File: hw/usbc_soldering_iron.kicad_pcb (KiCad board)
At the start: 4 copper layers, 70 x 30 mm, 82 parts, among them J1 U263-163N-4OS1735, J16 TIP_CONN, J2 DBG, J3 OLED, J4 GPIO, J5 DISP, Q1 AGM403AP, U1 SC7A20, U10 TPA191Ax, U2 CH32X035F8U6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

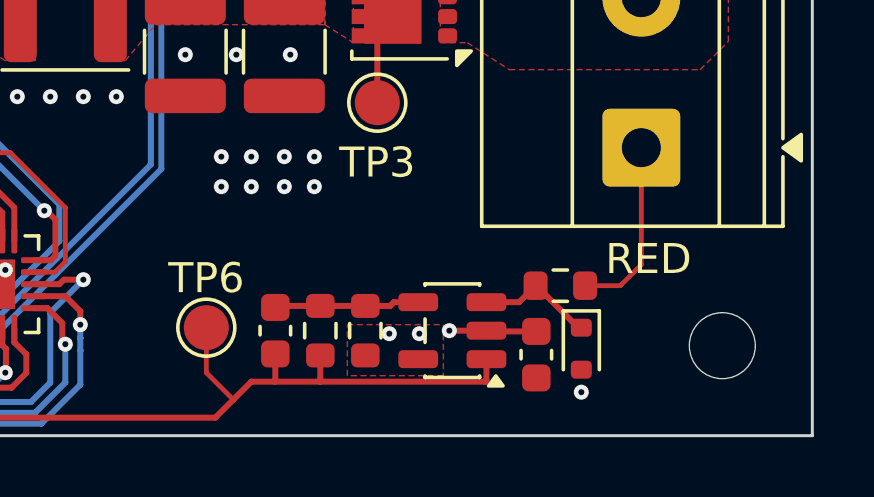
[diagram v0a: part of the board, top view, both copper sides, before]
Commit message: corrected tlv333 pin assignment
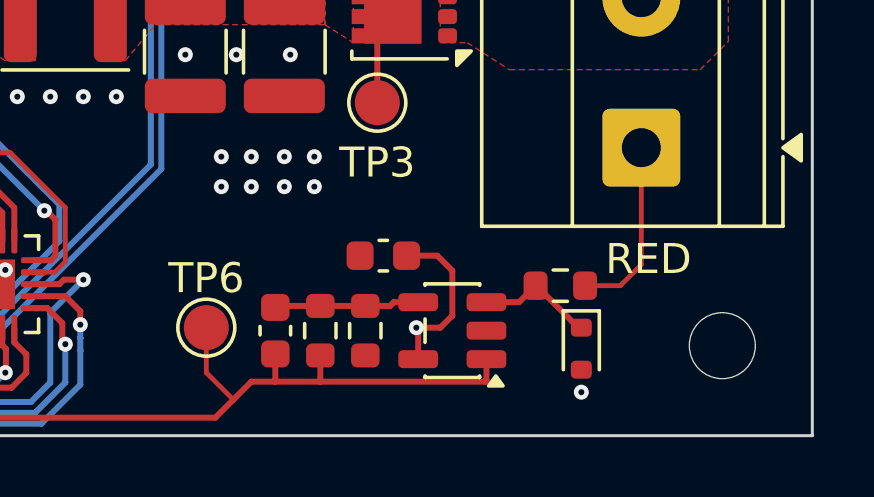
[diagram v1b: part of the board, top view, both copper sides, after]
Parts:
- moved C8 6.07 mm to (156.2, 152.2), turned to 180 degrees
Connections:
- U6 pad 2: +3.3V -> GND
- U6 pad 5: GND -> +3.3V
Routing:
- net +3.3V: track 184.1 -> 185.7 mm
- net GND: track 3.25 -> 3.29 mm, vias 81 -> 79
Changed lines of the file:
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@@
 			(unit
 				(name "A")
-				(pins "3" "4" "2" "5" "1")
+				(pins "3" "4" "5" "2" "1")
 			)
 		)
@@
 			(layers "F.Cu" "F.Mask" "F.Paste")
 			(roundrect_rratio 0.25)
-			(net "+3.3V")
-			(pinfunction "V+_2")
+			(net "GND")
+			(pinfunction "V-_2")
 			(pintype "power_in")
 		)
@@
 			(layers "F.Cu" "F.Mask" "F.Paste")
 			(roundrect_rratio 0.25)
-			(net "GND")
-			(pinfunction "V-_5")
+			(net "+3.3V")
+			(pinfunction "V+_5")
 			(pintype "power_in")
 		)
@@
 	(footprint "Capacitor_SMD:C_0603_1608Metric"
 		(layer "F.Cu")
-		(at 161.3 155.5 -90)
+		(at 156.2 152.2 180)
 		(descr "Capacitor SMD 0603 (1608 Metric), square (rectangular) end terminal, IPC-7351 nominal, (Body size source: IPC-SM-782 page 76, https://www.pcb-3d.com/wordpress/wp-content/uploads/ipc-sm-782a_amendment_1_and_2.pdf), generated with kicad-footprint-generator")
 		(tags "capacitor")
 		(property "Reference" "C8"
-			(at 0 -1.43 90)
+			(at 0 -1.43 0)
 			(layer "F.SilkS")
 			(hide yes)
@@
 		)
 		(property "Value" "100n"
-			(at 0 1.43 90)
+			(at 0 1.43 0)
 			(layer "F.Fab")
 			(effects
@@
 		)
 		(property "Datasheet" ""
-			(at 0 0 90)
+			(at 0 0 0)
 			(layer "F.Fab")
 			(hide yes)
@@
 		)
 		(property "Description" "Unpolarized capacitor, small symbol"
-			(at 0 0 90)
+			(at 0 0 0)
 			(layer "F.Fab")
 			(hide yes)
@@
 		)
 		(fp_text user "${REFERENCE}"
-			(at 0 0 90)
+			(at 0 0 0)
 			(layer "F.Fab")
 			(effects
@@
 		)
 		(pad "1" smd roundrect
-			(at -0.775 0 270)
+			(at -0.775 0 180)
 			(size 0.9 0.95)
 			(layers "F.Cu" "F.Mask" "F.Paste")
@@
 		)
 		(pad "2" smd roundrect
-			(at 0.775 0 270)
+			(at 0.775 0 180)
 			(size 0.9 0.95)
 			(layers "F.Cu" "F.Mask" "F.Paste")
@@
 	)
 	(segment
+		(start 157.3625 155.65)
+		(end 157.3625 154.6625)
+		(width 0.2)
+		(layer "F.Cu")
+		(net "+3.3V")
+	)
+	(segment
 		(start 134.6 135.6)
 		(end 139.1 135.6)
@@
 	)
 	(segment
+		(start 157.3625 154.6625)
+		(end 157.3 154.6)
+		(width 0.2)
+		(layer "F.Cu")
+		(net "+3.3V")
+	)
+	(segment
 		(start 131.6 130.35)
 		(end 132.55 129.4)
@@
 	)
 	(segment
-		(start 138.9 132.375)
-		(end 138.9 133.15)
+		(start 158 152.2)
+		(end 156.975 152.2)
 		(width 0.2)
 		(layer "F.Cu")
@@
 	)
 	(segment
-		(start 159.6625 154.725)
-		(end 159.6375 154.7)
+		(start 138.9 132.375)
+		(end 138.9 133.15)
 		(width 0.2)
 		(layer "F.Cu")
@@
 	)
 	(segment
+		(start 158.5 154.2)
+		(end 158.5 152.7)
+		(width 0.2)
+		(layer "F.Cu")
+		(net "+3.3V")
+	)
+	(segment
 		(start 142.2125 130.7)
 		(end 143 130.7)
@@
 	)
 	(segment
+		(start 158.1 154.6)
+		(end 158.5 154.2)
+		(width 0.2)
+		(layer "F.Cu")
+		(net "+3.3V")
+	)
+	(segment
 		(start 141.65 152.35)
 		(end 140.4 152.35)
@@
 	)
 	(segment
+		(start 158.5 152.7)
+		(end 158 152.2)
+		(width 0.2)
+		(layer "F.Cu")
+		(net "+3.3V")
+	)
+	(segment
 		(start 108.05 151.85)
 		(end 106.95 151.85)
@@
 	)
 	(segment
-		(start 161.3 154.725)
-		(end 159.6625 154.725)
-		(width 0.2)
-		(layer "F.Cu")
-		(net "+3.3V")
-	)
-	(segment
 		(start 131.6 132.5)
 		(end 131.6 130.35)
@@
 	)
 	(segment
-		(start 159.6375 154.7)
-		(end 158.4 154.7)
+		(start 157.3 154.6)
+		(end 158.1 154.6)
 		(width 0.2)
 		(layer "F.Cu")
@@
 	)
 	(via
-		(at 158.4 154.7)
+		(at 157.3 154.6)
 		(size 0.5)
 		(drill 0.2)
@@
 	)
 	(segment
-		(start 157.35 153.65)
-		(end 148.95 153.65)
-		(width 0.5)
-		(layer "In2.Cu")
-		(net "+3.3V")
-	)
-	(segment
 		(start 138.55 153.05)
 		(end 137.4 151.9)
@@
 	)
 	(segment
-		(start 114.6 156.1)
-		(end 114.6 154.6)
+		(start 157.3 154.6)
+		(end 156.4 154.6)
 		(width 0.5)
 		(layer "In2.Cu")
@@
 	)
 	(segment
-		(start 158.4 154.7)
-		(end 157.35 153.65)
+		(start 114.6 156.1)
+		(end 114.6 154.6)
 		(width 0.5)
 		(layer "In2.Cu")
@@
 	)
 	(segment
+		(start 155.45 153.65)
+		(end 148.95 153.65)
+		(width 0.5)
+		(layer "In2.Cu")
+		(net "+3.3V")
+	)
+	(segment
 		(start 119.54 144.36)
 		(end 124 139.9)
@@
 	)
 	(segment
+		(start 156.4 154.6)
+		(end 155.45 153.65)
+		(width 0.5)
+		(layer "In2.Cu")
+		(net "+3.3V")
+	)
+	(segment
 		(start 137.925 152.425)
 		(end 138.55 153.05)
@@
 	)
 	(segment
+		(start 159.6625 154.725)
+		(end 159.6375 154.7)
+		(width 0.2)
+		(layer "F.Cu")
+		(net "GND")
+	)
+	(segment
 		(start 153.5 132.7875)
 		(end 153.5 133.9)
@@
 	)
 	(via
-		(at 156.4 154.8)
-		(size 0.5)
-		(drill 0.2)
-		(layers "F.Cu" "B.Cu")
-		(free yes)
-		(capping no)
-		(covering
-			(front no)
-			(back no)
-		)
-		(plugging
-			(front no)
-			(back no)
-		)
-		(filling no)
-		(net "GND")
-	)
-	(via
 		(at 162.8 156.75)
 		(size 0.5)
@@
 	)
 	(via
-		(at 157.4 154.8)
-		(size 0.5)
-		(drill 0.2)
-		(layers "F.Cu" "B.Cu")
-		(free yes)
-		(capping no)
-		(covering
-			(front no)
-			(back no)
-		)
-		(plugging
-			(front no)
-			(back no)
-		)
-		(filling no)
-		(net "GND")
-	)
-	(via
 		(at 161.5 134)
 		(size 0.5)
@@
 	)
 	(zone
-		(net "GND")
-		(layer "F.Cu")
-		(hatch edge 0.5)
-		(priority 20)
-		(connect_pads
-			(clearance 0.2)
-		)
-		(min_thickness 0.1)
-		(fill yes
-			(thermal_gap 0.2)
-			(thermal_bridge_width 0.5)
-			(island_removal_mode 0)
-		)
-		(polygon
-			(pts
-				(xy 155 154.5) (xy 158.2 154.5) (xy 158.2 156.2) (xy 155 156.2)
-			)
-		)
-	)
-	(zone
 		(net "/BLUE")
 		(layer "F.Cu")
@@
 		)
 	)
-	(group ""
-		(members "2c622d7b-95ad-4ba0-85a5-6460405268bc" "32ad7a21-be26-49a9-bdca-adc0bc673893"
-			"3d4daa28-6462-482b-a696-2e00d7b2c7d1" "471808db-6b3f-4f3f-8f7f-7fadb6504455"
-			"484fa138-56a9-47f2-9876-244c74aa7e31" "49ea340c-e187-4bed-b6e8-4101b0b22fcd"
-			"4b6e41a1-5624-413d-95b0-1f5db6b59de1" "4d7d10ec-e601-46b8-bb2a-6c1f03bc9ede"
-			"563eb97b-7856-4b5e-bc8f-9e8f5bd48c32" "5e030718-43ba-4f5e-b2e3-1e2a28ee68ac"
-			"6257dbbf-128a-4dbd-abb0-00be223f8db8" "6562aa6b-9502-45be-a216-1d5c6d877d32"
-			"6b9c42e3-28c7-44cb-b3ae-7458845edf0b" "8eeff956-0efd-43b3-8705-91f384f4a736"
-			"952864cb-edb6-4f37-9761-5ba490c2aba2" "994dbc7d-cf30-4a21-9524-a5c8ed064a7c"
-			"a5a60eef-7a45-4eb8-9fa8-9f308154dcd8" "b08968d5-09ed-4ff5-bd39-d0896b5142c6"
-			"b4bddd41-0f24-4d04-9eb6-8f83b0044304" "b665c86d-ae65-43c3-af17-8db5633c4572"
-			"c5d7bdb2-5df7-4ce5-8a42-35ac0e1c4145" "d80e259f-fa1c-4c78-b98e-06df4d54ff7e"
-			"ee8c303c-4c6e-4fb9-8937-eacda85ca043" "f78962e1-0d6c-43b7-9602-0a021f5a94b3"
-			"fb46bc63-f400-4cd1-937e-31bae0861caa"
-		)
-	)

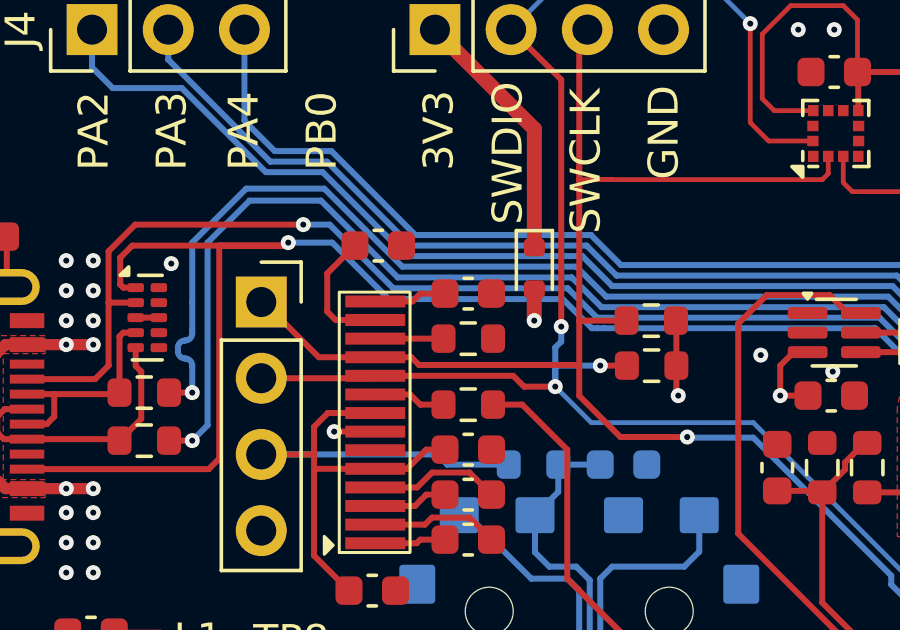
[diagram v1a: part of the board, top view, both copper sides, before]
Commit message: 5.1k resistors in cc1/2
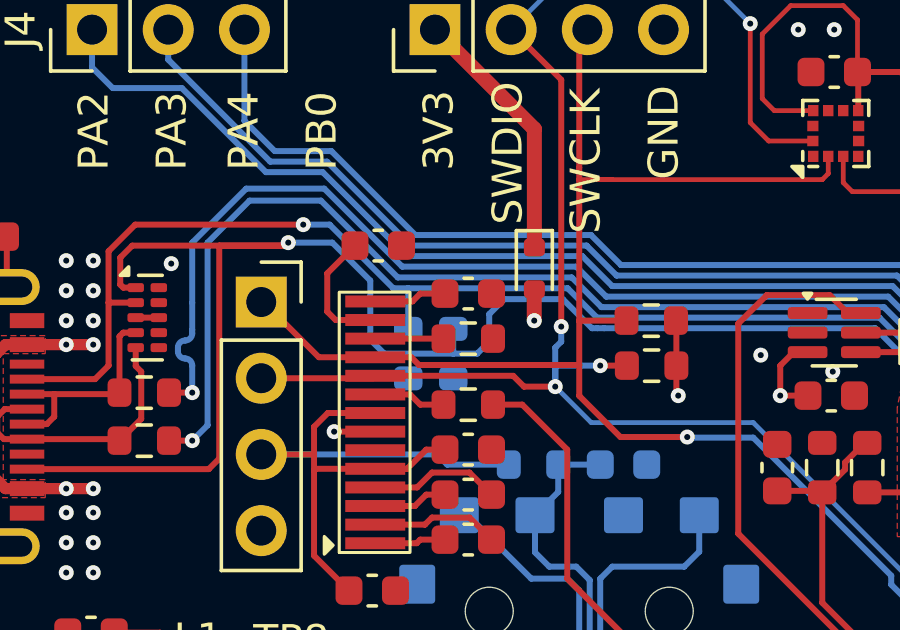
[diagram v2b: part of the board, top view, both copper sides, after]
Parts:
- added R18: 5.1k, Resistor_SMD:R_0603_1608Metric, B.Cu at (121.3, 141.0)
- added R19: 5.1k, Resistor_SMD:R_0603_1608Metric, B.Cu at (119.8, 141.0)
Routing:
- net /CC2: track 59.9 -> 63.9 mm
- net /CC1: track 51.0 -> 52.4 mm

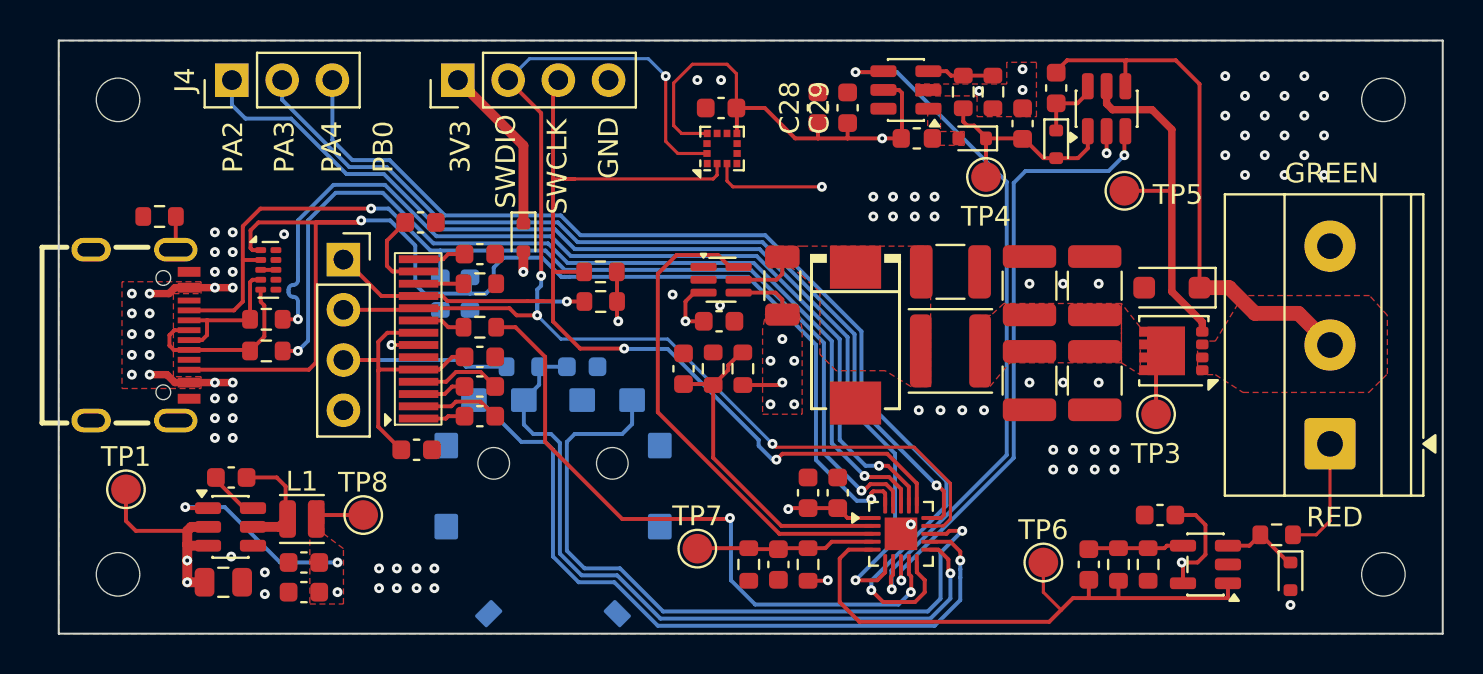
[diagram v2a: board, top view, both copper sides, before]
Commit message: debounce caps on encoder and silkscreen adj
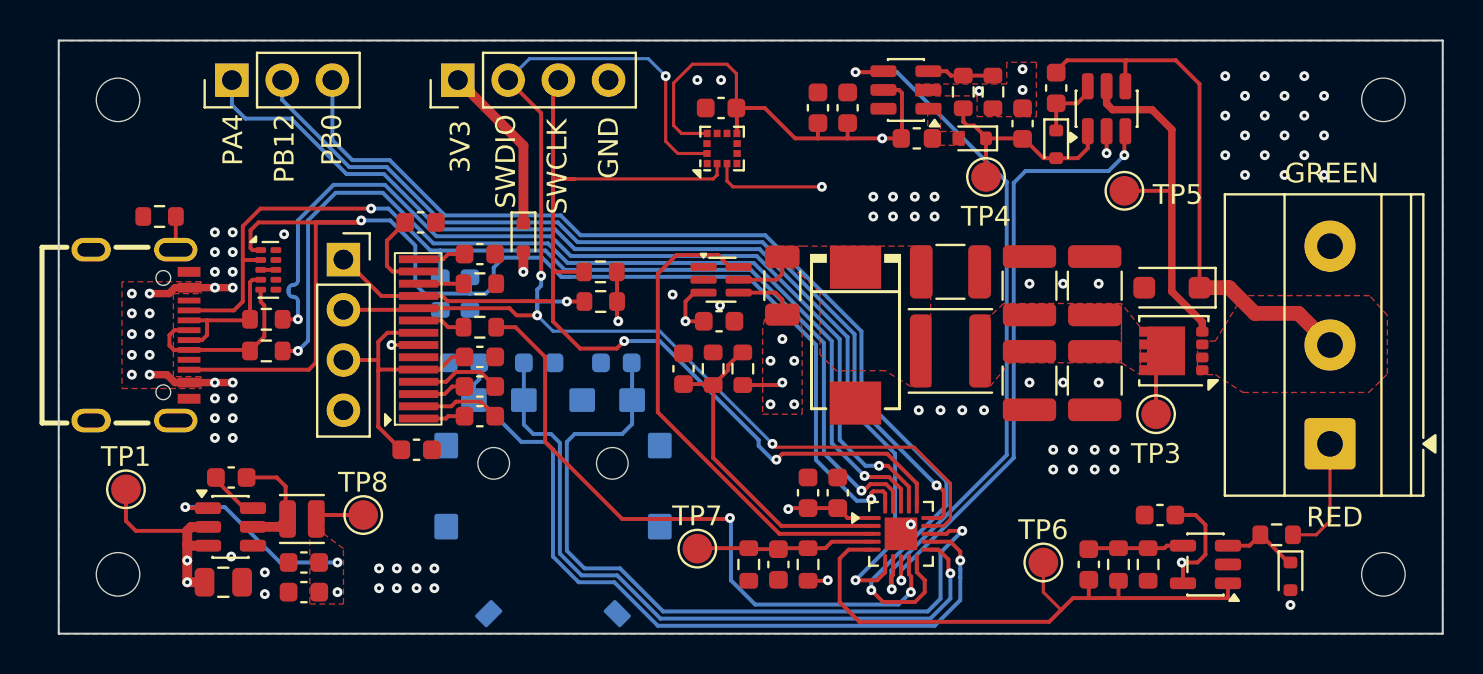
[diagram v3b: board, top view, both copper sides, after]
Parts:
- removed R7: 10k, Resistor_SMD:R_0603_1608Metric
- added C30: 100n, Capacitor_SMD:C_0603_1608Metric, B.Cu at (128.7, 144.5)
- added C31: 100n, Capacitor_SMD:C_0603_1608Metric, B.Cu at (121.0, 144.5)
- moved C6 2.18 mm to (124.8, 144.5)
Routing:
- net +3.3V: track 185.7 -> 177.3 mm
- net /ENC_A: track 37.2 -> 39.2 mm
- net /ENC_B: track 36.4 -> 38.3 mm
- net /BTN: track 37.2 -> 35.7 mm
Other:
- board text added: "PB12"
- board text removed: "PA2"
- board text removed: "PA3"

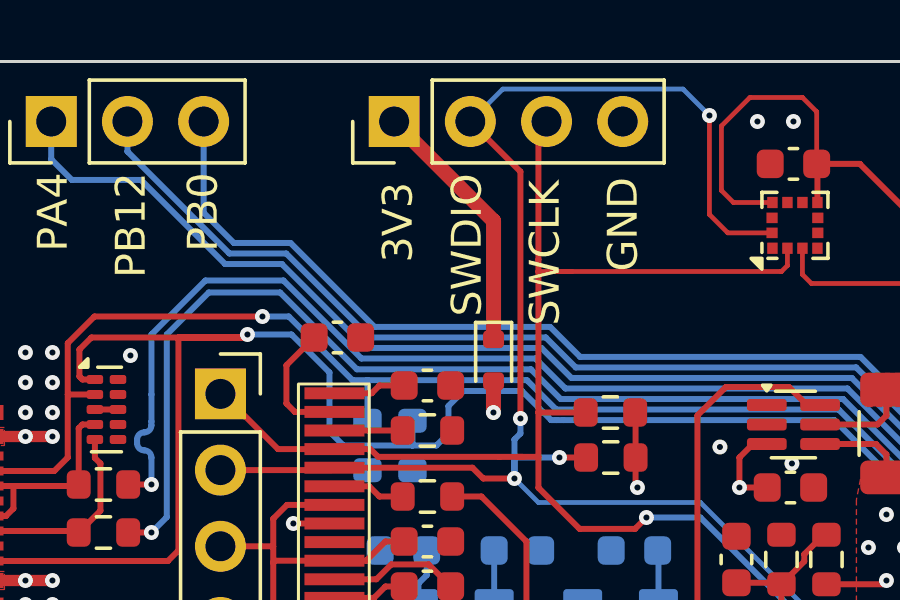
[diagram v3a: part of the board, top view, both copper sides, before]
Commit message: removed diode in programming header
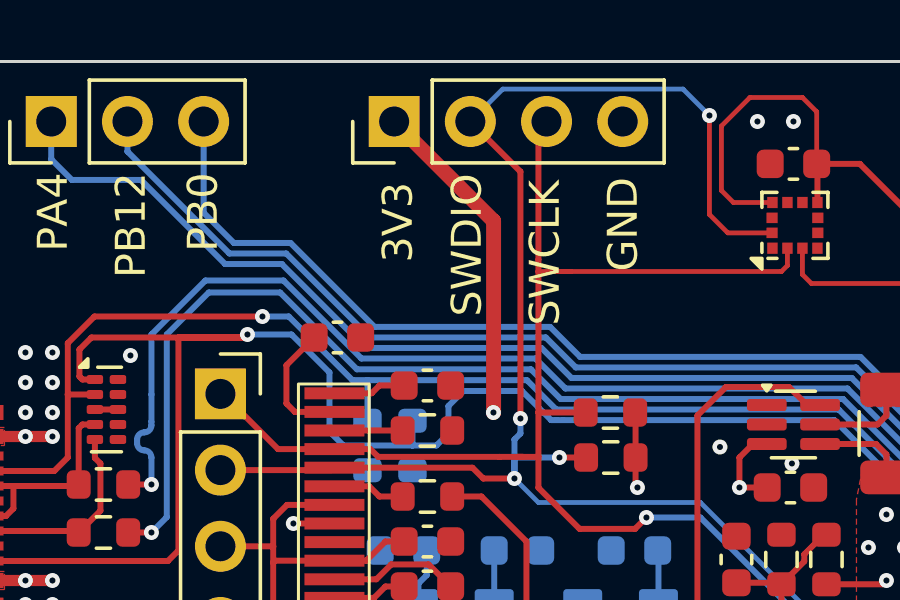
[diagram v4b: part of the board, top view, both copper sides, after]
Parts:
- removed D1: RB521S30T1G, Diode_SMD:D_SOD-523
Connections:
- J2 pad 1: Net-(D1-K) -> +3.3V
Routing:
- net +3.3V: track 177.3 -> 187.5 mm
- net Net-(D1-K): track 8.76 -> 0.00 mm

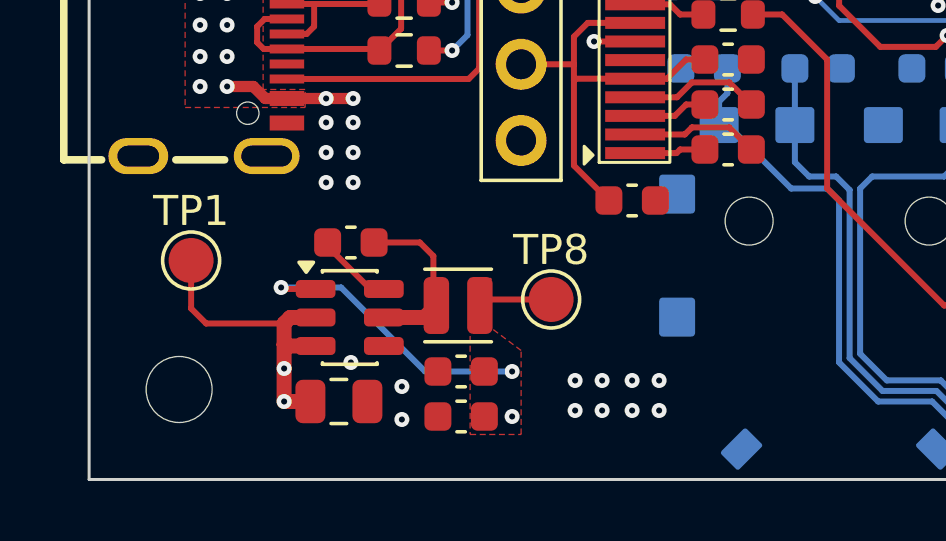
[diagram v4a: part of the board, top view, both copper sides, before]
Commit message: more capacitors in main buck
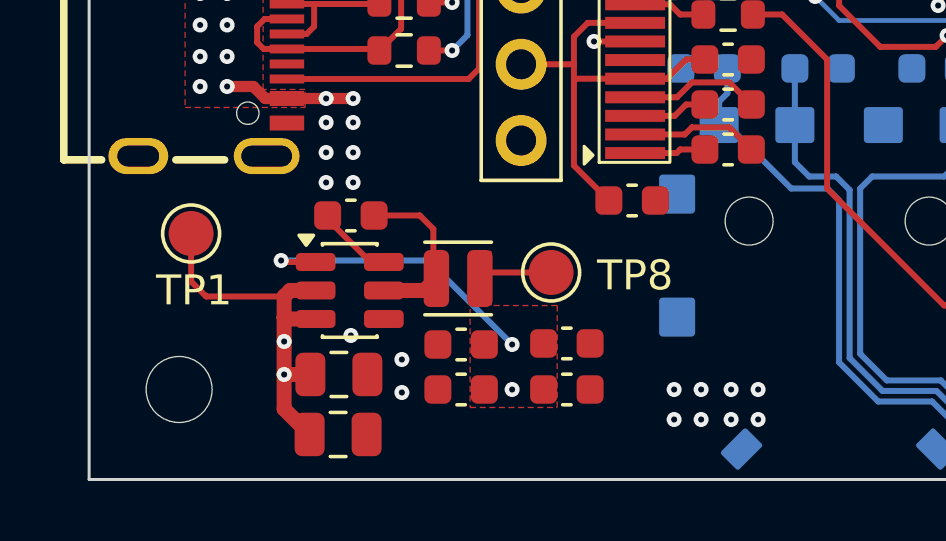
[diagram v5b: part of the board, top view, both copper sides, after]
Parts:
- added C32: 22u, Capacitor_SMD:C_0603_1608Metric, F.Cu at (116.4, 153.7)
- added C33: 22u, Capacitor_SMD:C_0603_1608Metric, F.Cu at (116.4, 155.2)
- added C34: 4.7u, Capacitor_SMD:C_0805_2012Metric, F.Cu at (108.8, 156.7)
- moved C11 0.90 mm to (112.9, 155.2)
- moved C5 0.90 mm to (108.8, 154.7)
- moved C7 0.90 mm to (109.2, 149.4)
- moved C9 0.90 mm to (112.9, 153.7)
- moved L1 0.90 mm to (112.8, 151.5)
- moved TP1 0.90 mm to (103.9, 150.0)
- moved U5 0.90 mm to (109.2, 151.9)
- moved TP8 0.90 mm to (115.9, 151.3)
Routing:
- net VBUS: track 35.0 -> 36.5 mm
